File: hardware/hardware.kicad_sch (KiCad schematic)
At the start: 152 parts, among them IC1 TPA3118D2DAPR, IC2 MAX98357AEWL+T, IC3 TAS5760LDAPR, IC4 TPS56A37RPAR, J1 Conn_01x02, J2 CONUFL001-SMD-T, J3 Conn_01x04_Socket, J4 GMC020080HR, J6 Conn_01x04_Socket, Q1 BC817, SW1 SW_Push, SW2 SW_Push, SW3 SW_Push, SW4 SW_Push, SW5 SW_Push, SW6 SW_Push, U1 ESP32-S3, U2 W25X40CLSV, U3 TPS563200, U4 W25X40CLSV, Y1 40MHz

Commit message: schematic - faltando o RTC clock, e conectar os I2C's num so canal
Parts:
- removed C19, C20, C25: 10uF, Capacitor_SMD:C_0805_2012Metric_Pad1.18x1.45mm_HandSolder, symbol Device:C_Small
- removed C21, C23: 0.1uF, Capacitor_SMD:C_0805_2012Metric_Pad1.18x1.45mm_HandSolder, symbol Device:C_Small
- removed C22: 47nF, Capacitor_SMD:C_0805_2012Metric_Pad1.18x1.45mm_HandSolder, symbol Device:C_Small
- removed C24, C27, C28, C29, C40, C41: 1uF, Capacitor_SMD:C_0805_2012Metric_Pad1.18x1.45mm_HandSolder, symbol Device:C_Small
- removed C30, C37, C42, C43: 1nF, Capacitor_SMD:C_0805_2012Metric_Pad1.18x1.45mm_HandSolder, symbol Device:C_Small
- removed C31, C38: 100nF, Capacitor_SMD:C_0805_2012Metric_Pad1.18x1.45mm_HandSolder, symbol Device:C_Small
- removed C32, C39: 220uF, symbol Device:C_Polarized_Small_US
- removed C33, C34, C35, C36: 220nF, Capacitor_SMD:C_0805_2012Metric_Pad1.18x1.45mm_HandSolder, symbol Device:C_Small
- removed C44, C45: 10nF, Capacitor_SMD:C_0805_2012Metric_Pad1.18x1.45mm_HandSolder, symbol Device:C_Small
- removed H1, H2, H3, H4: MountingHole, symbol Mechanical:MountingHole
- removed IC1: TPA3118D2DAPR, SOP65P810X120-33N, symbol TPA3118D2DAPR:TPA3118D2DAPR
- removed IC2: MAX98357AEWL+T, BGA9C40P3X3_144X135X69, symbol MAX98357AEWL+T:MAX98357AEWL+T
- removed IC4: TPS56A37RPAR, TPS56A37RPAR, symbol TPS56A37RPAR:TPS56A37RPAR
- removed J1: Conn_01x02, symbol Connector_Generic:Conn_01x02
- removed J2: CONUFL001-SMD-T, SnapEDA Library:LINX_CONUFL001-SMD-T, symbol CONUFL001-SMD-T:CONUFL001-SMD-T
- removed J3, J6: Conn_01x04_Socket, symbol Connector:Screw_Terminal_01x04
- removed L4, L6: 10uH, symbol Device:L
- removed L5: TBD, Diode_SMD:D_0805_2012Metric_Pad1.15x1.40mm_HandSolder, symbol Device:L_Small
- removed L9: 2.2uH, Diode_SMD:D_0805_2012Metric_Pad1.15x1.40mm_HandSolder, symbol Device:L_Small
- removed LS1, LS2: Speaker, symbol Device:Speaker
- removed Q1: BC817, Package_TO_SOT_SMD:SOT-23, symbol Transistor_BJT:BC817
- removed R10, R11, R17, R8, R9: 0R, Resistor_SMD:R_0805_2012Metric_Pad1.20x1.40mm_HandSolder, symbol Device:R_Small
- removed R12: 169K, Resistor_SMD:R_0805_2012Metric_Pad1.20x1.40mm_HandSolder, symbol Device:R_Small
- removed R13: 36.1K, Resistor_SMD:R_0805_2012Metric_Pad1.20x1.40mm_HandSolder, symbol Device:R_Small
- removed R14: 10K, Resistor_SMD:R_0805_2012Metric_Pad1.20x1.40mm_HandSolder, symbol Device:R_Small
- removed R15: 52.3K, Resistor_SMD:R_0805_2012Metric_Pad1.20x1.40mm_HandSolder, symbol Device:R_Small
- removed R16, R24, R27: 100K, Resistor_SMD:R_0805_2012Metric_Pad1.20x1.40mm_HandSolder, symbol Device:R_Small
- removed R25: 47K, Resistor_SMD:R_0805_2012Metric_Pad1.20x1.40mm_HandSolder, symbol Device:R_Small
- removed R26: 75K, Resistor_SMD:R_0805_2012Metric_Pad1.20x1.40mm_HandSolder, symbol Device:R_Small
- removed R28, R29: 3.3R, Resistor_SMD:R_0805_2012Metric_Pad1.20x1.40mm_HandSolder, symbol Device:R_Small
- removed U2, U4: W25X40CLSV, Package_SO:SOP-8_3.9x4.9mm_P1.27mm, symbol Memory_Flash:W25X40CLSV
- added ANT1: PCB_ANT, RF_Antenna:Texas_SWRA117D_2.4GHz_Left, symbol Rastreador_Library:PCB_ANT
- added C71, C72: TBD, Capacitor_SMD:C_0402_1005Metric, symbol Device:C_Small
- added J1, J2: Conn_01x04, Connector_PinHeader_1.27mm:PinHeader_1x04_P1.27mm_Vertical, symbol Connector_Generic:Conn_01x04
- added JP1, JP2, JP3, JP4: SolderJumper_2_Open, Jumper:SolderJumper-2_P1.3mm_Open_RoundedPad1.0x1.5mm, symbol Jumper:SolderJumper_2_Open
- added L4: 2.2uH, SamacSys_Parts:XEL4030101MED, symbol Device:L_Ferrite
- added Y2: 32.768KHz, symbol Device:Crystal_GND23
- C1, C2: value TBD -> 10pF; footprint Capacitor_SMD:C_0805_2012Metric_Pad1.18x1.45mm_HandSolder -> Capacitor_SMD:C_0402_1005Metric
- C10, C11, C12, C13, C14, C15, C16, C17, C18, C26, C3, C4, C46, C47, C48, C49, C5, C50, C51, C52, C53, C54, C55, C56, C57, C58, C59, C6, C60, C61, C62, C63, C64, C65, C66, C67, C68, C69, C7, C70, C8, C9: footprint Capacitor_SMD:C_0805_2012Metric_Pad1.18x1.45mm_HandSolder -> Capacitor_SMD:C_0402_1005Metric
- L1, L2, L3: footprint Diode_SMD:D_0805_2012Metric_Pad1.15x1.40mm_HandSolder -> Inductor_SMD:L_0402_1005Metric
- L7, L8: footprint (none) -> Inductor_SMD:L_0402_1005Metric
- LS3: footprint (none) -> Connector_PinSocket_2.54mm:PinSocket_2x01_P2.54mm_Vertical_SMD
- R1: value TBD -> 0R; footprint Resistor_SMD:R_0805_2012Metric_Pad1.20x1.40mm_HandSolder -> Resistor_SMD:R_0402_1005Metric
- R18, R19, R2, R20, R21, R22, R23, R3, R30, R31, R32, R33, R34, R35, R36, R37, R38, R39, R4, R40, R41, R42, R43, R5, R6: footprint Resistor_SMD:R_0805_2012Metric_Pad1.20x1.40mm_HandSolder -> Resistor_SMD:R_0402_1005Metric
- R7: value 0R -> TBD; footprint Resistor_SMD:R_0805_2012Metric_Pad1.20x1.40mm_HandSolder -> Resistor_SMD:R_0402_1005Metric
- SW1, SW2, SW3, SW4, SW5, SW6: footprint (none) -> Button_Switch_SMD:SW_SPST_PTS810
- Y1: footprint (none) -> Crystal:Crystal_SMD_2520-4Pin_2.5x2.0mm
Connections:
- net 3V3: now also U1.6 (GPIO1), J1.1 (Pin_1), J2.3 (Pin_3), L4.2
- net AUDIO_CLK: now also U1.11 (GPIO6)
- net AUDIO_EN: now also U1.7 (GPIO2)
- net AUDIO_MUTE: now also U1.10 (GPIO5)
- net BT_E: now also U1.25 (GPIO19/USB_D-); no longer U1.11 (GPIO6)
- net BT_N: now also U1.23 (GPIO17); no longer U1.9 (GPIO4)
- net BT_S: now also U1.24 (GPIO18); no longer U1.10 (GPIO5)
- net BT_W: now also U1.26 (GPIO20/USB_D+); no longer U1.12 (GPIO7)
- net Display_SCL: now also U1.28 (SPICS1), J2.2 (Pin_2); no longer U1.14 (GPIO9)
- net Display_SDA: now also U1.27 (GPIO21), J2.1 (Pin_1); no longer U1.13 (GPIO8)
- net GND: now also C71.1, C72.2
- net GND_E: now also J4.MP4 (WP_PIN), U1.57 (GND), ANT1.2, J1.4 (Pin_4), J2.4 (Pin_4), Y2.2, Y2.3
- net I2C_CLK: now also U1.12 (GPIO7)
- net I2C_DATA_IN: now also U1.9 (GPIO4)
- net LED_B: now also U1.45 (MTDO)
- net LED_G: now also U1.44 (MTCK)
- net LED_R: now also U1.43 (GPIO38)
- net LRCK: now also U1.14 (GPIO9)
- net RX0: now also J1.2 (Pin_2)
- net SDIN: now also U1.13 (GPIO8)
- net TX0: now also J1.3 (Pin_3)
- net at C50.1, L8.2, LS3.2: now also JP1.1 (A), JP2.1 (A); no longer C62.1, R38.2
- net at C52.2, U3.2 (SW): now also L4.1
- net at C14.2, L2.1, L3.1: now also ANT1.1
- net at C48.2, L7.2, LS3.1: now also JP3.2 (B), JP4.2 (B); no longer C61.2, R37.1
- net at U1.21 (XTAL_32K_P): now also C71.2, Y2.1
- net at U1.22 (XTAL_32K_N): now also R7.2
- net at U1.35 (SPID): no longer R7.2
- net SPI_CS: no longer names the net of U1.32 (SPICS0)
- net SPI_DI: no longer names the net of R7.1
- net SPI_DI: now also C72.1, Y2.4
- new net: C61.2, JP3.1 (A)
- new net: JP4.1 (A), R37.1
- new net: JP1.2 (B), R38.2
- new net: C62.1, JP2.2 (B)
- no-connect marks 10 -> 21
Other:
- note added: "Micro-SD"
- note removed: "Flash 3V3 4MB"
- note removed: "Memories"
- note removed: "PSRAM 3V3 2MB"
- note removed: "PVC Decoupling"
- note removed: "Regulador de Tensão"
- note removed: "micro SD"
- moved on the sheet: BT1, C1, C10, C11, C12, C13, C14, C15, C17, C18, C2, C26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

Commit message: atualizando alguns footprints; começando o desenho da placa
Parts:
- C15: renamed from C52; footprint Capacitor_SMD:C_0402_1005Metric -> Capacitor_SMD:C_0805_2012Metric_Pad1.18x1.45mm_HandSolder
- C17: renamed from C53; footprint Capacitor_SMD:C_0402_1005Metric -> Capacitor_SMD:C_0603_1608Metric_Pad1.08x0.95mm_HandSolder
- C20: renamed from C54; footprint Capacitor_SMD:C_0402_1005Metric -> Capacitor_SMD:C_0603_1608Metric_Pad1.08x0.95mm_HandSolder
- C21: renamed from C60; footprint Capacitor_SMD:C_0402_1005Metric -> Capacitor_SMD:C_0603_1608Metric_Pad1.08x0.95mm_HandSolder
- C6: renamed from C66; footprint Capacitor_SMD:C_0402_1005Metric -> Capacitor_SMD:C_0805_2012Metric_Pad1.18x1.45mm_HandSolder
- C8: renamed from C65; footprint Capacitor_SMD:C_0402_1005Metric -> Capacitor_SMD:C_0805_2012Metric_Pad1.18x1.45mm_HandSolder
- D1: renamed from D2; footprint (none) -> Connector_PinHeader_1.27mm:PinHeader_1x04_P1.27mm_Vertical_SMD_Pin1Left
- IC1: renamed from IC3; footprint SOP65P810X120-33N -> Package_SO:HTSSOP-32-1EP_6.1x11mm_P0.65mm_EP5.2x11mm_Mask4.11x4.36mm_ThermalVias
- L4: footprint SamacSys_Parts:XEL4030101MED -> Inductor_SMD:L_TDK_VLS6045EX_VLS6045AF
- R10: renamed from R31; footprint Resistor_SMD:R_0402_1005Metric -> Resistor_SMD:R_0201_0603Metric_Pad0.64x0.40mm_HandSolder
- R11: renamed from R32; footprint Resistor_SMD:R_0402_1005Metric -> Resistor_SMD:R_0201_0603Metric_Pad0.64x0.40mm_HandSolder
- R12: renamed from R36; footprint Resistor_SMD:R_0402_1005Metric -> Resistor_SMD:R_0201_0603Metric_Pad0.64x0.40mm_HandSolder
- R13: renamed from R33; footprint Resistor_SMD:R_0402_1005Metric -> Resistor_SMD:R_0201_0603Metric_Pad0.64x0.40mm_HandSolder
- R14: renamed from R35; footprint Resistor_SMD:R_0402_1005Metric -> Resistor_SMD:R_0201_0603Metric_Pad0.64x0.40mm_HandSolder
- R15: renamed from R34; footprint Resistor_SMD:R_0402_1005Metric -> Resistor_SMD:R_0201_0603Metric_Pad0.64x0.40mm_HandSolder
- R16: renamed from R40; footprint Resistor_SMD:R_0402_1005Metric -> Resistor_SMD:R_0201_0603Metric_Pad0.64x0.40mm_HandSolder
- R20: renamed from R41; footprint Resistor_SMD:R_0402_1005Metric -> Resistor_SMD:R_0201_0603Metric_Pad0.64x0.40mm_HandSolder
- R22: renamed from R42; footprint Resistor_SMD:R_0402_1005Metric -> Resistor_SMD:R_0201_0603Metric_Pad0.64x0.40mm_HandSolder
- R26: renamed from R43; footprint Resistor_SMD:R_0402_1005Metric -> Resistor_SMD:R_0201_0603Metric_Pad0.64x0.40mm_HandSolder
- R27: renamed from R6; footprint Resistor_SMD:R_0402_1005Metric -> Resistor_SMD:R_0201_0603Metric_Pad0.64x0.40mm_HandSolder
- R5: renamed from R39; footprint Resistor_SMD:R_0402_1005Metric -> Resistor_SMD:R_0201_0603Metric_Pad0.64x0.40mm_HandSolder
- renumbered C15 to C1, C6 to C10, C51 to C11, C7 to C12, C1 to C13, C2 to C14, C8 to C16, C72 to C18, C71 to C19, C14 to C2, C3 to C22, C4 to C23, C5 to C24, C57 to C25, C55 to C26, C56 to C27, C67 to C28, C46 to C29, C9 to C3, C17 to C30, C18 to C31, C47 to C32, C49 to C33, C68 to C34, C48 to C35, C50 to C36, C26 to C37, C59 to C38, C58 to C39, C13 to C4, C61 to C40, C62 to C41, C69 to C42, C63 to C43, C64 to C44, C16 to C45, C70 to C46, C10 to C5, C12 to C7, C11 to C9, J4 to J1, J1 to J2, J2 to J3, JP3 to JP1, JP4 to JP3, JP1 to JP4, L3 to L1, L1 to L3, L7 to L5, L8 to L6, LS3 to LS1, R3 to R1, R18 to R17, R19 to R18, R20 to R19, R22 to R2, R5 to R21, R37 to R23, R38 to R24, R4 to R25, R21 to R3, R23 to R4, R1 to R6, R2 to R8, R30 to R9, SW3 to SW1, SW4 to SW2, SW1 to SW3, SW5 to SW4, SW2 to SW5, U3 to U1, U1 to U2

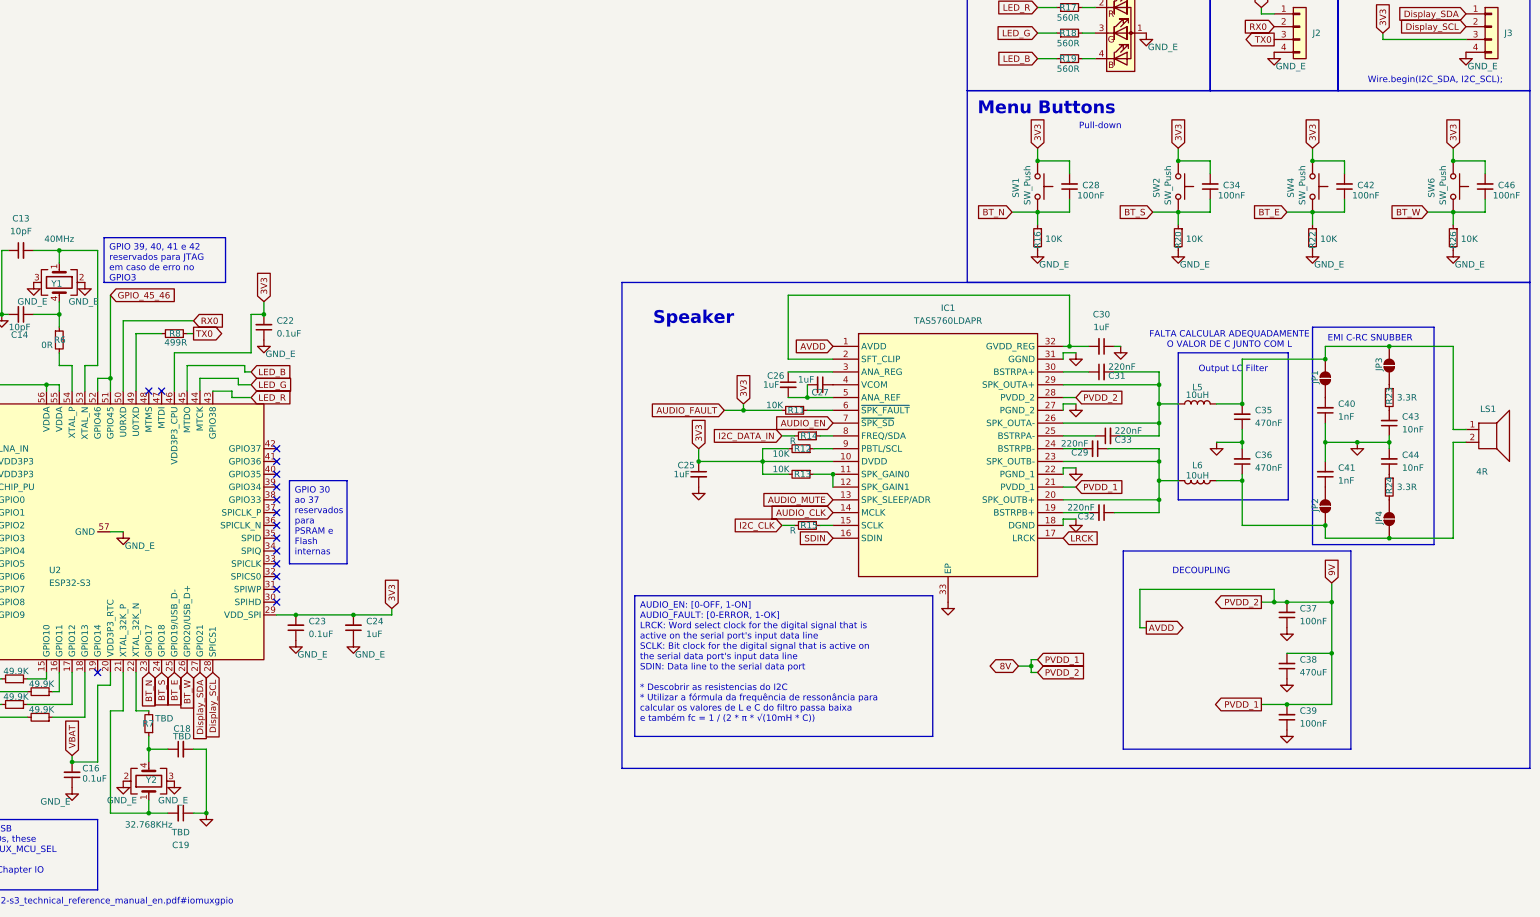
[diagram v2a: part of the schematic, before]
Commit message: RTC footprint; removed 2 buttons, an will remove more stuff to get the USB back
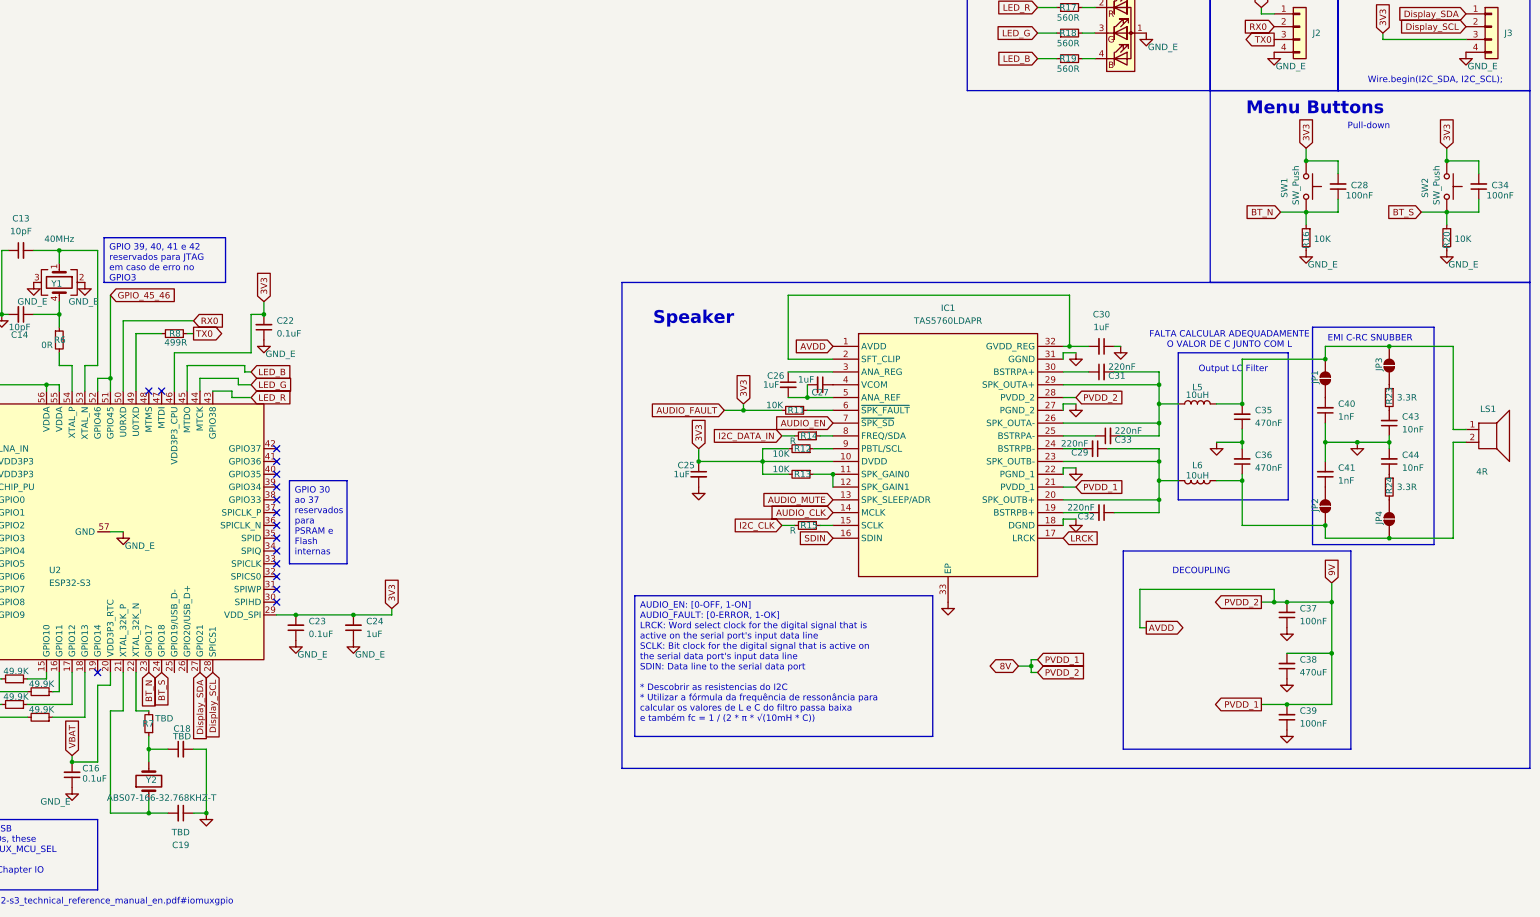
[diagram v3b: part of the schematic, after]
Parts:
- removed C42, C46: 100nF, Capacitor_SMD:C_0402_1005Metric, symbol Device:C_Small
- removed R22, R26: 10K, Resistor_SMD:R_0201_0603Metric_Pad0.64x0.40mm_HandSolder, symbol Device:R_Small
- removed SW4, SW6: SW_Push, Button_Switch_SMD:SW_SPST_PTS810, symbol Switch:SW_Push
- Y2: value 32.768KHz -> ABS07-166-32.768KHZ-T; footprint (none) -> Crystal:Crystal_SMD_MicroCrystal_CC7V-T1A-2Pin_3.2x1.5mm_HandSoldering; symbol Device:Crystal_GND23 -> Device:Crystal
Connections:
- net GND_E: no longer Y2.2, Y2.3
- net at C18.1, R7.1: now also Y2.2; no longer Y2.4
- net BT_E: no longer names the net of U2.25 (GPIO19/USB_D-)
- net BT_W: no longer names the net of U2.26 (GPIO20/USB_D+)
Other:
- moved on the sheet: C28, C34, R16, R20, SW1, SW2
